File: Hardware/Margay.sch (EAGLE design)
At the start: 79 parts, among them J1 SDMMC06132, J3 CONN_6SCREW_2.54, Q1 DMG3404, Q2 FDN360P, Q3 2N7002, U1 ATMEGA1284M, U10 TLV3691DPF, U11 MIC94090C6, U12 BME280, U13 MAX6070AAUT18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

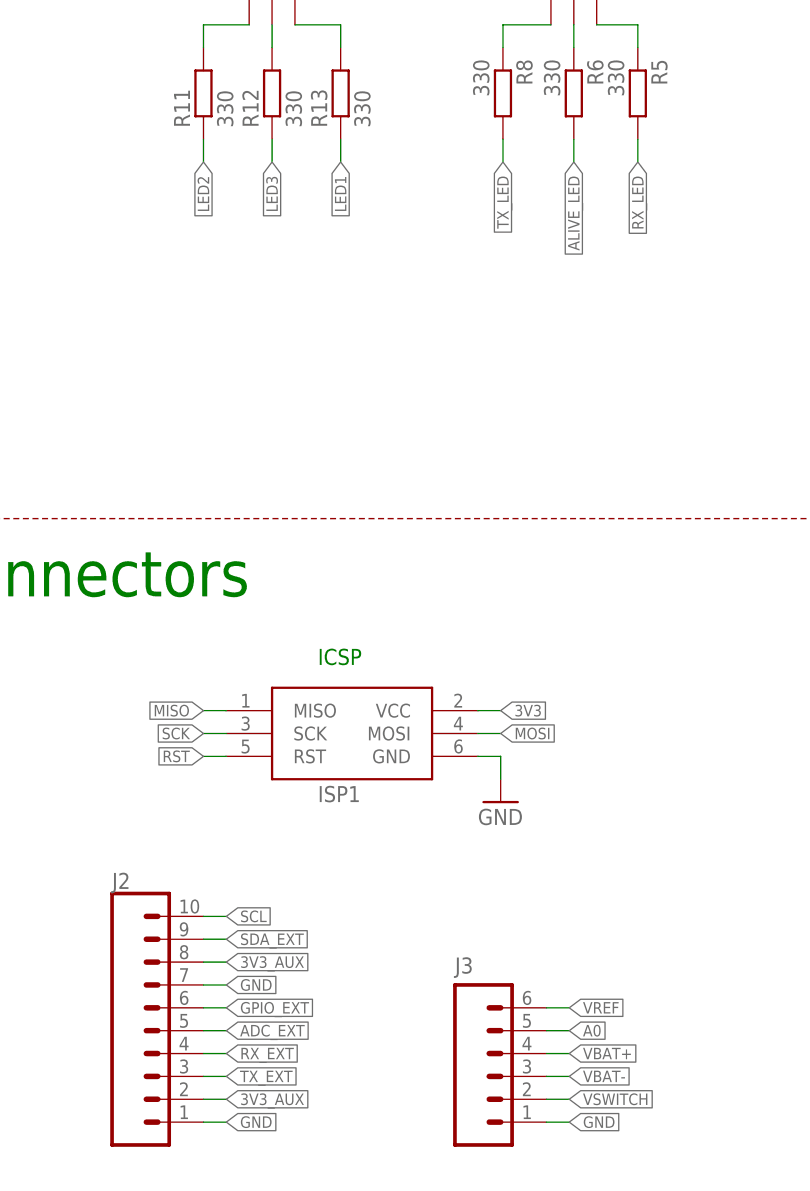
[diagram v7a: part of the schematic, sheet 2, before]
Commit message: Update wire names: match code and silk
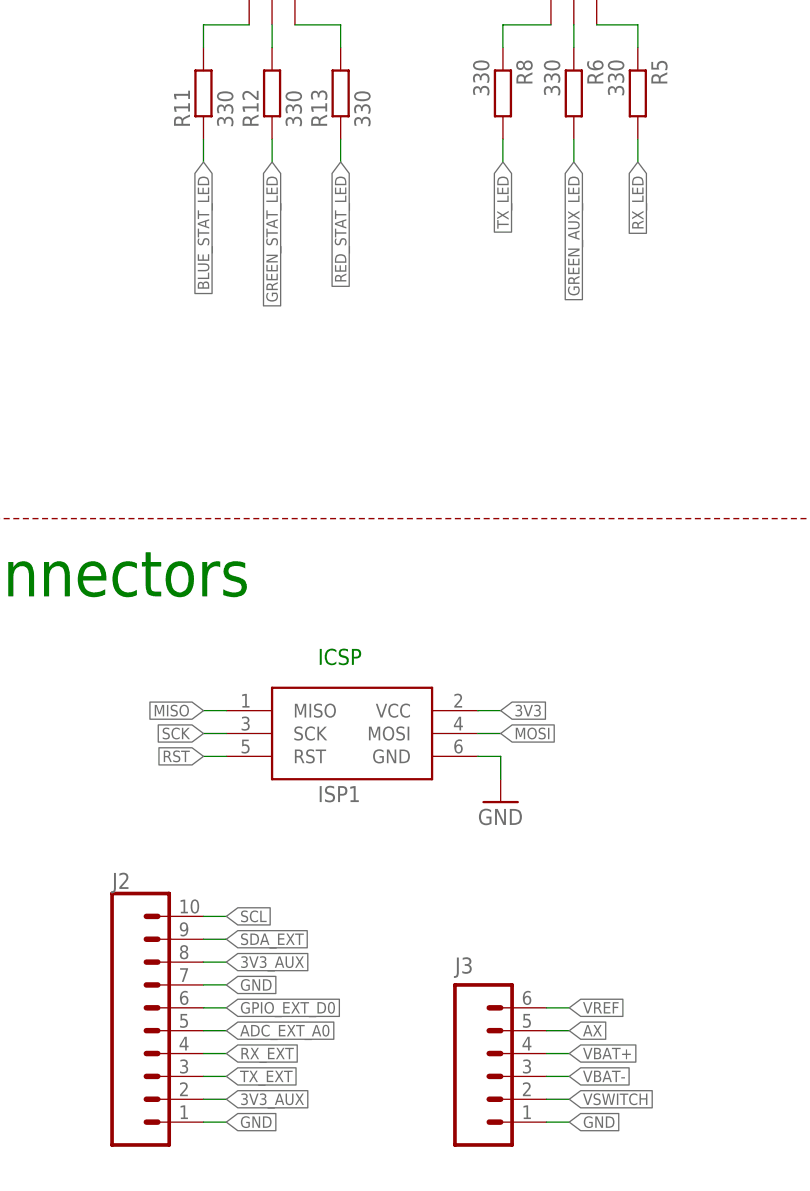
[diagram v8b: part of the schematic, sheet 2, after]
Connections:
- net A0 renamed AX
- net ADC_EXT renamed ADC_EXT_A0
- net ALIVE_LED renamed GREEN_AUX_LED
- net GPIO_EXT renamed GPIO_EXT_D0
- net LED1 renamed RED_STAT_LED
- net LED2 renamed BLUE_STAT_LED
- net LED3 renamed GREEN_STAT_LED
- net N$1 renamed _GREEN_AUX_LED
- net N$10 renamed _GREEN_STAT_LED
- net N$13 renamed VDIV_AX
- net N$15 renamed _RED_STAT_LED
- net N$16 renamed _RED_TX_AUX_LED
- net N$26 renamed _BLUE_RX_AUX_LED
- net N$31 renamed VCOIN+
- net N$5 renamed XTAL2
- net N$8 renamed XTAL1
- net N$9 renamed _BLUE_STAT_LED
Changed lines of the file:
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@@
 <?xml version="1.0" encoding="utf-8"?>
 <!DOCTYPE eagle SYSTEM "eagle.dtd">
-<eagle version="9.6.1">
+<eagle version="9.6.2">
 <drawing>
 <settings>
-<setting alwaysvectorfont="no"/>
+<setting alwaysvectorfont="yes"/>
 <setting verticaltext="up"/>
 </settings>
@@
 </segment>
 </net>
-<net name="N$5" class="0">
+<net name="XTAL2" class="0">
 <segment>
 <pinref part="XTAL1" gate="G$1" pin="2"/>
@@
 </segment>
 </net>
-<net name="N$8" class="0">
+<net name="XTAL1" class="0">
 <segment>
 <pinref part="C3" gate="G$1" pin="2"/>
@@
 </segment>
 </net>
-<net name="LED3" class="0">
+<net name="GREEN_STAT_LED" class="0">
 <segment>
 <pinref part="U1" gate="G$1" pin="(PCINT31/OC2A)PD7"/>
@@
 </segment>
 </net>
-<net name="LED1" class="0">
+<net name="RED_STAT_LED" class="0">
 <segment>
 <pinref part="U1" gate="G$1" pin="(PCINT29/OC1A)PD5"/>
@@
 </segment>
 </net>
-<net name="LED2" class="0">
+<net name="BLUE_STAT_LED" class="0">
 <segment>
 <pinref part="U1" gate="G$1" pin="(PCINT30/OC2B/ICP)PD6"/>
@@
 </segment>
 </net>
-<net name="ALIVE_LED" class="0">
+<net name="GREEN_AUX_LED" class="0">
 <segment>
 <wire x1="109.22" y1="50.8" x2="111.76" y2="50.8" width="0.1524" layer="91"/>
@@
 </segment>
 </net>
-<net name="GPIO_EXT" class="0">
+<net name="GPIO_EXT_D0" class="0">
 <segment>
 <pinref part="U1" gate="G$1" pin="(PCINT11/OC0A/AIN1)PB3"/>
@@
 </segment>
 </net>
-<net name="ADC_EXT" class="0">
+<net name="ADC_EXT_A0" class="0">
 <segment>
 <pinref part="U1" gate="G$1" pin="(PCINT0/ADC0)PA0"/>
@@
 </segment>
 </net>
-<net name="GPIO_EXT" class="0">
+<net name="GPIO_EXT_D0" class="0">
 <segment>
 <wire x1="40.64" y1="30.48" x2="43.18" y2="30.48" width="0.1524" layer="91"/>
@@
 </segment>
 </net>
-<net name="A0" class="0">
+<net name="AX" class="0">
 <segment>
 <wire x1="78.74" y1="27.94" x2="81.28" y2="27.94" width="0.1524" layer="91"/>
@@
 </segment>
 </net>
-<net name="N$9" class="0">
+<net name="_BLUE_STAT_LED" class="0">
 <segment>
 <pinref part="R11" gate="G$1" pin="2"/>
@@
 </segment>
 </net>
-<net name="N$10" class="0">
+<net name="_GREEN_STAT_LED" class="0">
 <segment>
 <pinref part="R12" gate="G$1" pin="2"/>
@@
 </segment>
 </net>
-<net name="N$15" class="0">
+<net name="_RED_STAT_LED" class="0">
 <segment>
 <pinref part="D3" gate="G$1" pin="RED_CATH"/>
@@
 </segment>
 </net>
-<net name="LED3" class="0">
+<net name="GREEN_STAT_LED" class="0">
 <segment>
 <pinref part="R12" gate="G$1" pin="1"/>
@@
 </segment>
 </net>
-<net name="LED1" class="0">
+<net name="RED_STAT_LED" class="0">
 <segment>
 <pinref part="R13" gate="G$1" pin="1"/>
@@
 </segment>
 </net>
-<net name="LED2" class="0">
+<net name="BLUE_STAT_LED" class="0">
 <segment>
 <pinref part="R11" gate="G$1" pin="1"/>
@@
 </segment>
 </net>
-<net name="ADC_EXT" class="0">
+<net name="ADC_EXT_A0" class="0">
 <segment>
 <wire x1="40.64" y1="27.94" x2="43.18" y2="27.94" width="0.1524" layer="91"/>
@@
 </segment>
 </net>
-<net name="N$16" class="0">
+<net name="_RED_TX_AUX_LED" class="0">
 <segment>
 <pinref part="R8" gate="G$1" pin="1"/>
@@
 </segment>
 </net>
-<net name="N$26" class="0">
+<net name="_BLUE_RX_AUX_LED" class="0">
 <segment>
 <pinref part="D2" gate="G$1" pin="BLUE_CATH"/>
@@
 </segment>
 </net>
-<net name="ALIVE_LED" class="0">
+<net name="GREEN_AUX_LED" class="0">
 <segment>
 <pinref part="R6" gate="G$1" pin="2"/>
@@
 </segment>
 </net>
-<net name="N$1" class="0">
+<net name="_GREEN_AUX_LED" class="0">
 <segment>
 <pinref part="D2" gate="G$1" pin="GREEN_CATH"/>
@@
 </segment>
 </net>
-<net name="N$31" class="0">
+<net name="VCOIN+" class="0">
 <segment>
 <pinref part="RTC1" gate="G$1" pin="VBAT"/>
@@
 </segment>
 </net>
-<net name="N$13" class="0">
+<net name="VDIV_AX" class="0">
 <segment>
 <pinref part="JP3" gate="G$1" pin="2"/>
@@
 </segment>
 </net>
-<net name="A0" class="0">
+<net name="AX" class="0">
 <segment>
 <pinref part="U14" gate="G$1" pin="VIN+"/>
